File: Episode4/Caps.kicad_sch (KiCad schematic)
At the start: 170 parts

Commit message: Worked on BOM
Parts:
- added C176, C177, C183: 470µF, Capacitor_SMD:CP_Elec_16x17.5, symbol Device:C_Polarized_US
- added C178, C179, C184, C188, C191: 1µF, Capacitor_SMD:C_0805_2012Metric_Pad1.18x1.45mm_HandSolder, symbol Device:C_Small
- added C180, C181, C182, C185, C186, C189, C192: .1µF, Capacitor_SMD:C_0805_2012Metric_Pad1.18x1.45mm_HandSolder, symbol Device:C_Small
- added C187, C190: 100µF, Capacitor_SMD:CP_Elec_10x7.7, symbol Device:C_Polarized_US
- added C6: 1000µF, Capacitor_SMD:CP_Elec_16x17.5, symbol Device:C_Polarized_US
- C10: renamed from C9; footprint Capacitor_THT:C_Disc_D3.4mm_W2.1mm_P2.50mm -> Capacitor_SMD:C_0805_2012Metric_Pad1.18x1.45mm_HandSolder; Manufacturer_Name (none) -> Samsung Electro-Mechanics; Manufacturer_Part_Number (none) -> CL21B104KBFNNNG
- C100: renamed from C99; footprint Capacitor_THT:C_Disc_D3.4mm_W2.1mm_P2.50mm -> Capacitor_SMD:C_0805_2012Metric_Pad1.18x1.45mm_HandSolder; Manufacturer_Name (none) -> Samsung Electro-Mechanics; Manufacturer_Part_Number (none) -> CL21B104KBFNNNG
- C101: renamed from C100; footprint Capacitor_THT:C_Disc_D3.4mm_W2.1mm_P2.50mm -> Capacitor_SMD:C_0805_2012Metric_Pad1.18x1.45mm_HandSolder; Manufacturer_Name (none) -> Samsung Electro-Mechanics; Manufacturer_Part_Number (none) -> CL21B104KBFNNNG
- C102: renamed from C101; footprint Capacitor_THT:C_Disc_D3.4mm_W2.1mm_P2.50mm -> Capacitor_SMD:C_0805_2012Metric_Pad1.18x1.45mm_HandSolder; Manufacturer_Name (none) -> Samsung Electro-Mechanics; Manufacturer_Part_Number (none) -> CL21B104KBFNNNG
- C103: renamed from C102; footprint Capacitor_THT:C_Disc_D3.4mm_W2.1mm_P2.50mm -> Capacitor_SMD:C_0805_2012Metric_Pad1.18x1.45mm_HandSolder; Manufacturer_Name (none) -> Samsung Electro-Mechanics; Manufacturer_Part_Number (none) -> CL21B104KBFNNNG
- C104: renamed from C103; footprint Capacitor_THT:C_Disc_D3.4mm_W2.1mm_P2.50mm -> Capacitor_SMD:C_0805_2012Metric_Pad1.18x1.45mm_HandSolder; Manufacturer_Name (none) -> Samsung Electro-Mechanics; Manufacturer_Part_Number (none) -> CL21B104KBFNNNG
- C105: renamed from C104; footprint Capacitor_THT:C_Disc_D3.4mm_W2.1mm_P2.50mm -> Capacitor_SMD:C_0805_2012Metric_Pad1.18x1.45mm_HandSolder; Manufacturer_Name (none) -> Samsung Electro-Mechanics; Manufacturer_Part_Number (none) -> CL21B104KBFNNNG
- C106: renamed from C105; footprint Capacitor_THT:C_Disc_D3.4mm_W2.1mm_P2.50mm -> Capacitor_SMD:C_0805_2012Metric_Pad1.18x1.45mm_HandSolder; Manufacturer_Name (none) -> Samsung Electro-Mechanics; Manufacturer_Part_Number (none) -> CL21B104KBFNNNG
- C107: renamed from C106; footprint Capacitor_THT:C_Disc_D3.4mm_W2.1mm_P2.50mm -> Capacitor_SMD:C_0805_2012Metric_Pad1.18x1.45mm_HandSolder; Manufacturer_Name (none) -> Samsung Electro-Mechanics; Manufacturer_Part_Number (none) -> CL21B104KBFNNNG
- C108: renamed from C107; footprint Capacitor_THT:C_Disc_D3.4mm_W2.1mm_P2.50mm -> Capacitor_SMD:C_0805_2012Metric_Pad1.18x1.45mm_HandSolder; Manufacturer_Name (none) -> Samsung Electro-Mechanics; Manufacturer_Part_Number (none) -> CL21B104KBFNNNG
- C109: renamed from C108; footprint Capacitor_THT:C_Disc_D3.4mm_W2.1mm_P2.50mm -> Capacitor_SMD:C_0805_2012Metric_Pad1.18x1.45mm_HandSolder; Manufacturer_Name (none) -> Samsung Electro-Mechanics; Manufacturer_Part_Number (none) -> CL21B104KBFNNNG
- C11: renamed from C10; footprint Capacitor_THT:C_Disc_D3.4mm_W2.1mm_P2.50mm -> Capacitor_SMD:C_0805_2012Metric_Pad1.18x1.45mm_HandSolder; Manufacturer_Name (none) -> Samsung Electro-Mechanics; Manufacturer_Part_Number (none) -> CL21B104KBFNNNG
- C110: renamed from C109; footprint Capacitor_THT:C_Disc_D3.4mm_W2.1mm_P2.50mm -> Capacitor_SMD:C_0805_2012Metric_Pad1.18x1.45mm_HandSolder; Manufacturer_Name (none) -> Samsung Electro-Mechanics; Manufacturer_Part_Number (none) -> CL21B104KBFNNNG
- C111: renamed from C110; footprint Capacitor_THT:C_Disc_D3.4mm_W2.1mm_P2.50mm -> Capacitor_SMD:C_0805_2012Metric_Pad1.18x1.45mm_HandSolder; Manufacturer_Name (none) -> Samsung Electro-Mechanics; Manufacturer_Part_Number (none) -> CL21B104KBFNNNG
- C112: renamed from C111; footprint Capacitor_THT:C_Disc_D3.4mm_W2.1mm_P2.50mm -> Capacitor_SMD:C_0805_2012Metric_Pad1.18x1.45mm_HandSolder; Manufacturer_Name (none) -> Samsung Electro-Mechanics; Manufacturer_Part_Number (none) -> CL21B104KBFNNNG
- C113: renamed from C112; footprint Capacitor_THT:C_Disc_D3.4mm_W2.1mm_P2.50mm -> Capacitor_SMD:C_0805_2012Metric_Pad1.18x1.45mm_HandSolder; Manufacturer_Name (none) -> Samsung Electro-Mechanics; Manufacturer_Part_Number (none) -> CL21B104KBFNNNG
- C114: renamed from C113; footprint Capacitor_THT:C_Disc_D3.4mm_W2.1mm_P2.50mm -> Capacitor_SMD:C_0805_2012Metric_Pad1.18x1.45mm_HandSolder; Manufacturer_Name (none) -> Samsung Electro-Mechanics; Manufacturer_Part_Number (none) -> CL21B104KBFNNNG
- C115: renamed from C114; footprint Capacitor_THT:C_Disc_D3.4mm_W2.1mm_P2.50mm -> Capacitor_SMD:C_0805_2012Metric_Pad1.18x1.45mm_HandSolder; Manufacturer_Name (none) -> Samsung Electro-Mechanics; Manufacturer_Part_Number (none) -> CL21B104KBFNNNG
- C116: renamed from C115; footprint Capacitor_THT:C_Disc_D3.4mm_W2.1mm_P2.50mm -> Capacitor_SMD:C_0805_2012Metric_Pad1.18x1.45mm_HandSolder; Manufacturer_Name (none) -> Samsung Electro-Mechanics; Manufacturer_Part_Number (none) -> CL21B104KBFNNNG
- C117: renamed from C116; footprint Capacitor_THT:C_Disc_D3.4mm_W2.1mm_P2.50mm -> Capacitor_SMD:C_0805_2012Metric_Pad1.18x1.45mm_HandSolder; Manufacturer_Name (none) -> Samsung Electro-Mechanics; Manufacturer_Part_Number (none) -> CL21B104KBFNNNG
- C118: renamed from C117; footprint Capacitor_THT:C_Disc_D3.4mm_W2.1mm_P2.50mm -> Capacitor_SMD:C_0805_2012Metric_Pad1.18x1.45mm_HandSolder; Manufacturer_Name (none) -> Samsung Electro-Mechanics; Manufacturer_Part_Number (none) -> CL21B104KBFNNNG
- C119: renamed from C118; footprint Capacitor_THT:C_Disc_D3.4mm_W2.1mm_P2.50mm -> Capacitor_SMD:C_0805_2012Metric_Pad1.18x1.45mm_HandSolder; Manufacturer_Name (none) -> Samsung Electro-Mechanics; Manufacturer_Part_Number (none) -> CL21B104KBFNNNG
- C12: renamed from C11; value 100µF -> 470µF; footprint Capacitor_THT:CP_Radial_D6.3mm_P2.50mm -> Capacitor_SMD:CP_Elec_16x17.5; Manufacturer_Name (none) -> Nichicon; Manufacturer_Part_Number (none) -> UCD1H471MNJ1MS
- C120: renamed from C119; footprint Capacitor_THT:C_Disc_D3.4mm_W2.1mm_P2.50mm -> Capacitor_SMD:C_0805_2012Metric_Pad1.18x1.45mm_HandSolder; Manufacturer_Name (none) -> Samsung Electro-Mechanics; Manufacturer_Part_Number (none) -> CL21B104KBFNNNG
- C121: renamed from C120; footprint Capacitor_THT:C_Disc_D3.4mm_W2.1mm_P2.50mm -> Capacitor_SMD:C_0805_2012Metric_Pad1.18x1.45mm_HandSolder; Manufacturer_Name (none) -> Samsung Electro-Mechanics; Manufacturer_Part_Number (none) -> CL21B104KBFNNNG
- C122: renamed from C121; footprint Capacitor_THT:C_Disc_D3.4mm_W2.1mm_P2.50mm -> Capacitor_SMD:C_0805_2012Metric_Pad1.18x1.45mm_HandSolder; Manufacturer_Name (none) -> Samsung Electro-Mechanics; Manufacturer_Part_Number (none) -> CL21B104KBFNNNG
- C123: renamed from C122; footprint Capacitor_THT:C_Disc_D3.4mm_W2.1mm_P2.50mm -> Capacitor_SMD:C_0805_2012Metric_Pad1.18x1.45mm_HandSolder; Manufacturer_Name (none) -> Samsung Electro-Mechanics; Manufacturer_Part_Number (none) -> CL21B104KBFNNNG
- C124: renamed from C123; footprint Capacitor_THT:C_Disc_D3.4mm_W2.1mm_P2.50mm -> Capacitor_SMD:C_0805_2012Metric_Pad1.18x1.45mm_HandSolder; Manufacturer_Name (none) -> Samsung Electro-Mechanics; Manufacturer_Part_Number (none) -> CL21B104KBFNNNG
- C125: renamed from C124; footprint Capacitor_THT:C_Disc_D3.4mm_W2.1mm_P2.50mm -> Capacitor_SMD:C_0805_2012Metric_Pad1.18x1.45mm_HandSolder; Manufacturer_Name (none) -> Samsung Electro-Mechanics; Manufacturer_Part_Number (none) -> CL21B104KBFNNNG
- C126: renamed from C125; footprint Capacitor_THT:C_Disc_D3.4mm_W2.1mm_P2.50mm -> Capacitor_SMD:C_0805_2012Metric_Pad1.18x1.45mm_HandSolder; Manufacturer_Name (none) -> Samsung Electro-Mechanics; Manufacturer_Part_Number (none) -> CL21B104KBFNNNG
- C127: renamed from C126; footprint Capacitor_THT:C_Disc_D3.4mm_W2.1mm_P2.50mm -> Capacitor_SMD:C_0805_2012Metric_Pad1.18x1.45mm_HandSolder; Manufacturer_Name (none) -> Samsung Electro-Mechanics; Manufacturer_Part_Number (none) -> CL21B104KBFNNNG
- C128: renamed from C127; footprint Capacitor_THT:C_Disc_D3.4mm_W2.1mm_P2.50mm -> Capacitor_SMD:C_0805_2012Metric_Pad1.18x1.45mm_HandSolder; Manufacturer_Name (none) -> Samsung Electro-Mechanics; Manufacturer_Part_Number (none) -> CL21B104KBFNNNG
- C129: renamed from C128; footprint Capacitor_THT:C_Disc_D3.4mm_W2.1mm_P2.50mm -> Capacitor_SMD:C_0805_2012Metric_Pad1.18x1.45mm_HandSolder; Manufacturer_Name (none) -> Samsung Electro-Mechanics; Manufacturer_Part_Number (none) -> CL21B104KBFNNNG
- C13: renamed from C12; footprint Capacitor_THT:C_Disc_D3.4mm_W2.1mm_P2.50mm -> Capacitor_SMD:C_0805_2012Metric_Pad1.18x1.45mm_HandSolder; Manufacturer_Name (none) -> Samsung Electro-Mechanics; Manufacturer_Part_Number (none) -> CL21B105KBFNNNG
- C130: renamed from C129; footprint Capacitor_THT:C_Disc_D3.4mm_W2.1mm_P2.50mm -> Capacitor_SMD:C_0805_2012Metric_Pad1.18x1.45mm_HandSolder; Manufacturer_Name (none) -> Samsung Electro-Mechanics; Manufacturer_Part_Number (none) -> CL21B104KBFNNNG
- C131: renamed from C130; footprint Capacitor_THT:C_Disc_D3.4mm_W2.1mm_P2.50mm -> Capacitor_SMD:C_0805_2012Metric_Pad1.18x1.45mm_HandSolder; Manufacturer_Name (none) -> Samsung Electro-Mechanics; Manufacturer_Part_Number (none) -> CL21B104KBFNNNG
- C132: renamed from C131; footprint Capacitor_THT:C_Disc_D3.4mm_W2.1mm_P2.50mm -> Capacitor_SMD:C_0805_2012Metric_Pad1.18x1.45mm_HandSolder; Manufacturer_Name (none) -> Samsung Electro-Mechanics; Manufacturer_Part_Number (none) -> CL21B105KBFNNNG
- C133: renamed from C132; footprint Capacitor_THT:C_Disc_D3.4mm_W2.1mm_P2.50mm -> Capacitor_SMD:C_0805_2012Metric_Pad1.18x1.45mm_HandSolder; Manufacturer_Name (none) -> Samsung Electro-Mechanics; Manufacturer_Part_Number (none) -> CL21B105KBFNNNG
- C134: renamed from C133; footprint Capacitor_THT:C_Disc_D3.4mm_W2.1mm_P2.50mm -> Capacitor_SMD:C_0805_2012Metric_Pad1.18x1.45mm_HandSolder; Manufacturer_Name (none) -> Samsung Electro-Mechanics; Manufacturer_Part_Number (none) -> CL21B105KBFNNNG
- C135: renamed from C134; footprint Capacitor_THT:C_Disc_D3.4mm_W2.1mm_P2.50mm -> Capacitor_SMD:C_0805_2012Metric_Pad1.18x1.45mm_HandSolder; Manufacturer_Name (none) -> Samsung Electro-Mechanics; Manufacturer_Part_Number (none) -> CL21B105KBFNNNG
- C136: renamed from C135; footprint Capacitor_THT:C_Disc_D3.4mm_W2.1mm_P2.50mm -> Capacitor_SMD:C_0805_2012Metric_Pad1.18x1.45mm_HandSolder; Manufacturer_Name (none) -> Samsung Electro-Mechanics; Manufacturer_Part_Number (none) -> CL21B105KBFNNNG
- C137: renamed from C136; footprint Capacitor_THT:C_Disc_D3.4mm_W2.1mm_P2.50mm -> Capacitor_SMD:C_0805_2012Metric_Pad1.18x1.45mm_HandSolder; Manufacturer_Name (none) -> Samsung Electro-Mechanics; Manufacturer_Part_Number (none) -> CL21B105KBFNNNG
- C138: renamed from C137; footprint Capacitor_THT:C_Disc_D3.4mm_W2.1mm_P2.50mm -> Capacitor_SMD:C_0805_2012Metric_Pad1.18x1.45mm_HandSolder; Manufacturer_Name (none) -> Samsung Electro-Mechanics; Manufacturer_Part_Number (none) -> CL21B105KBFNNNG
- C139: renamed from C138; footprint Capacitor_THT:C_Disc_D3.4mm_W2.1mm_P2.50mm -> Capacitor_SMD:C_0805_2012Metric_Pad1.18x1.45mm_HandSolder; Manufacturer_Name (none) -> Samsung Electro-Mechanics; Manufacturer_Part_Number (none) -> CL21B105KBFNNNG
- C14: renamed from C13; footprint Capacitor_THT:C_Disc_D3.4mm_W2.1mm_P2.50mm -> Capacitor_SMD:C_0805_2012Metric_Pad1.18x1.45mm_HandSolder; Manufacturer_Name (none) -> Samsung Electro-Mechanics; Manufacturer_Part_Number (none) -> CL21B104KBFNNNG
- C140: renamed from C139; footprint Capacitor_THT:C_Disc_D3.4mm_W2.1mm_P2.50mm -> Capacitor_SMD:C_0805_2012Metric_Pad1.18x1.45mm_HandSolder; Manufacturer_Name (none) -> Samsung Electro-Mechanics; Manufacturer_Part_Number (none) -> CL21B105KBFNNNG
- C141: renamed from C140; footprint Capacitor_THT:C_Disc_D3.4mm_W2.1mm_P2.50mm -> Capacitor_SMD:C_0805_2012Metric_Pad1.18x1.45mm_HandSolder; Manufacturer_Name (none) -> Samsung Electro-Mechanics; Manufacturer_Part_Number (none) -> CL21B105KBFNNNG
- C142: renamed from C141; footprint Capacitor_THT:C_Disc_D3.4mm_W2.1mm_P2.50mm -> Capacitor_SMD:C_0805_2012Metric_Pad1.18x1.45mm_HandSolder; Manufacturer_Name (none) -> Samsung Electro-Mechanics; Manufacturer_Part_Number (none) -> CL21B105KBFNNNG
- C143: renamed from C142; footprint Capacitor_THT:C_Disc_D3.4mm_W2.1mm_P2.50mm -> Capacitor_SMD:C_0805_2012Metric_Pad1.18x1.45mm_HandSolder; Manufacturer_Name (none) -> Samsung Electro-Mechanics; Manufacturer_Part_Number (none) -> CL21B104KBFNNNG
- C144: renamed from C143; footprint Capacitor_THT:C_Disc_D3.4mm_W2.1mm_P2.50mm -> Capacitor_SMD:C_0805_2012Metric_Pad1.18x1.45mm_HandSolder; Manufacturer_Name (none) -> Samsung Electro-Mechanics; Manufacturer_Part_Number (none) -> CL21B104KBFNNNG
- C145: renamed from C144; footprint Capacitor_THT:C_Disc_D3.4mm_W2.1mm_P2.50mm -> Capacitor_SMD:C_0805_2012Metric_Pad1.18x1.45mm_HandSolder; Manufacturer_Name (none) -> Samsung Electro-Mechanics; Manufacturer_Part_Number (none) -> CL21B104KBFNNNG
- C146: renamed from C145; footprint Capacitor_THT:C_Disc_D3.4mm_W2.1mm_P2.50mm -> Capacitor_SMD:C_0805_2012Metric_Pad1.18x1.45mm_HandSolder; Manufacturer_Name (none) -> Samsung Electro-Mechanics; Manufacturer_Part_Number (none) -> CL21B104KBFNNNG
- C147: renamed from C146; footprint Capacitor_THT:C_Disc_D3.4mm_W2.1mm_P2.50mm -> Capacitor_SMD:C_0805_2012Metric_Pad1.18x1.45mm_HandSolder; Manufacturer_Name (none) -> Samsung Electro-Mechanics; Manufacturer_Part_Number (none) -> CL21B104KBFNNNG
- C148: renamed from C147; footprint Capacitor_THT:C_Disc_D3.4mm_W2.1mm_P2.50mm -> Capacitor_SMD:C_0805_2012Metric_Pad1.18x1.45mm_HandSolder; Manufacturer_Name (none) -> Samsung Electro-Mechanics; Manufacturer_Part_Number (none) -> CL21B104KBFNNNG
- C149: renamed from C148; footprint Capacitor_THT:C_Disc_D3.4mm_W2.1mm_P2.50mm -> Capacitor_SMD:C_0805_2012Metric_Pad1.18x1.45mm_HandSolder; Manufacturer_Name (none) -> Samsung Electro-Mechanics; Manufacturer_Part_Number (none) -> CL21B104KBFNNNG
- C15: renamed from C14; footprint Capacitor_THT:C_Disc_D3.4mm_W2.1mm_P2.50mm -> Capacitor_SMD:C_0805_2012Metric_Pad1.18x1.45mm_HandSolder; Manufacturer_Name (none) -> Samsung Electro-Mechanics; Manufacturer_Part_Number (none) -> CL21B104KBFNNNG
- C150: renamed from C149; footprint Capacitor_THT:C_Disc_D3.4mm_W2.1mm_P2.50mm -> Capacitor_SMD:C_0805_2012Metric_Pad1.18x1.45mm_HandSolder; Manufacturer_Name (none) -> Samsung Electro-Mechanics; Manufacturer_Part_Number (none) -> CL21B104KBFNNNG
- C151: renamed from C150; footprint Capacitor_THT:C_Disc_D3.4mm_W2.1mm_P2.50mm -> Capacitor_SMD:C_0805_2012Metric_Pad1.18x1.45mm_HandSolder; Manufacturer_Name (none) -> Samsung Electro-Mechanics; Manufacturer_Part_Number (none) -> CL21B104KBFNNNG
- C152: renamed from C151; footprint Capacitor_THT:C_Disc_D3.4mm_W2.1mm_P2.50mm -> Capacitor_SMD:C_0805_2012Metric_Pad1.18x1.45mm_HandSolder; Manufacturer_Name (none) -> Samsung Electro-Mechanics; Manufacturer_Part_Number (none) -> CL21B104KBFNNNG
- C153: renamed from C152; footprint Capacitor_THT:C_Disc_D3.4mm_W2.1mm_P2.50mm -> Capacitor_SMD:C_0805_2012Metric_Pad1.18x1.45mm_HandSolder; Manufacturer_Name (none) -> Samsung Electro-Mechanics; Manufacturer_Part_Number (none) -> CL21B104KBFNNNG
- C154: renamed from C153; footprint Capacitor_THT:C_Disc_D3.4mm_W2.1mm_P2.50mm -> Capacitor_SMD:C_0805_2012Metric_Pad1.18x1.45mm_HandSolder; Manufacturer_Name (none) -> Samsung Electro-Mechanics; Manufacturer_Part_Number (none) -> CL21B105KBFNNNG
- C155: renamed from C154; footprint Capacitor_THT:C_Disc_D3.4mm_W2.1mm_P2.50mm -> Capacitor_SMD:C_0805_2012Metric_Pad1.18x1.45mm_HandSolder; Manufacturer_Name (none) -> Samsung Electro-Mechanics; Manufacturer_Part_Number (none) -> CL21B105KBFNNNG
- C156: renamed from C155; footprint Capacitor_THT:C_Disc_D3.4mm_W2.1mm_P2.50mm -> Capacitor_SMD:C_0805_2012Metric_Pad1.18x1.45mm_HandSolder; Manufacturer_Name (none) -> Samsung Electro-Mechanics; Manufacturer_Part_Number (none) -> CL21B105KBFNNNG
- C157: renamed from C156; footprint Capacitor_THT:C_Disc_D3.4mm_W2.1mm_P2.50mm -> Capacitor_SMD:C_0805_2012Metric_Pad1.18x1.45mm_HandSolder; Manufacturer_Name (none) -> Samsung Electro-Mechanics; Manufacturer_Part_Number (none) -> CL21B105KBFNNNG
- C158: renamed from C157; footprint Capacitor_THT:C_Disc_D3.4mm_W2.1mm_P2.50mm -> Capacitor_SMD:C_0805_2012Metric_Pad1.18x1.45mm_HandSolder; Manufacturer_Name (none) -> Samsung Electro-Mechanics; Manufacturer_Part_Number (none) -> CL21B105KBFNNNG
- C159: renamed from C158; footprint Capacitor_THT:C_Disc_D3.4mm_W2.1mm_P2.50mm -> Capacitor_SMD:C_0805_2012Metric_Pad1.18x1.45mm_HandSolder; Manufacturer_Name (none) -> Samsung Electro-Mechanics; Manufacturer_Part_Number (none) -> CL21B105KBFNNNG
- C16: renamed from C15; footprint Capacitor_THT:CP_Radial_D6.3mm_P2.50mm -> Capacitor_SMD:CP_Elec_10x7.7; Manufacturer_Name (none) -> Nichicon; Manufacturer_Part_Number (none) -> UCD1H101MCL6GS
- C160: renamed from C159; footprint Capacitor_THT:C_Disc_D3.4mm_W2.1mm_P2.50mm -> Capacitor_SMD:C_0805_2012Metric_Pad1.18x1.45mm_HandSolder; Manufacturer_Name (none) -> Samsung Electro-Mechanics; Manufacturer_Part_Number (none) -> CL21B105KBFNNNG
- C161: renamed from C160; footprint Capacitor_THT:C_Disc_D3.4mm_W2.1mm_P2.50mm -> Capacitor_SMD:C_0805_2012Metric_Pad1.18x1.45mm_HandSolder; Manufacturer_Name (none) -> Samsung Electro-Mechanics; Manufacturer_Part_Number (none) -> CL21B105KBFNNNG
- C162: renamed from C161; footprint Capacitor_THT:C_Disc_D3.4mm_W2.1mm_P2.50mm -> Capacitor_SMD:C_0805_2012Metric_Pad1.18x1.45mm_HandSolder; Manufacturer_Name (none) -> Samsung Electro-Mechanics; Manufacturer_Part_Number (none) -> CL21B105KBFNNNG
- C163: renamed from C162; footprint Capacitor_THT:C_Disc_D3.4mm_W2.1mm_P2.50mm -> Capacitor_SMD:C_0805_2012Metric_Pad1.18x1.45mm_HandSolder; Manufacturer_Name (none) -> Samsung Electro-Mechanics; Manufacturer_Part_Number (none) -> CL21B105KBFNNNG
- C164: renamed from C163; footprint Capacitor_THT:C_Disc_D3.4mm_W2.1mm_P2.50mm -> Capacitor_SMD:C_0805_2012Metric_Pad1.18x1.45mm_HandSolder; Manufacturer_Name (none) -> Samsung Electro-Mechanics; Manufacturer_Part_Number (none) -> CL21B105KBFNNNG
- C165: renamed from C164; footprint Capacitor_THT:C_Disc_D3.4mm_W2.1mm_P2.50mm -> Capacitor_SMD:C_0805_2012Metric_Pad1.18x1.45mm_HandSolder; Manufacturer_Name (none) -> Samsung Electro-Mechanics; Manufacturer_Part_Number (none) -> CL21B104KBFNNNG
- C166: renamed from C165; footprint Capacitor_THT:C_Disc_D3.4mm_W2.1mm_P2.50mm -> Capacitor_SMD:C_0805_2012Metric_Pad1.18x1.45mm_HandSolder; Manufacturer_Name (none) -> Samsung Electro-Mechanics; Manufacturer_Part_Number (none) -> CL21B104KBFNNNG
- C167: renamed from C166; footprint Capacitor_THT:C_Disc_D3.4mm_W2.1mm_P2.50mm -> Capacitor_SMD:C_0805_2012Metric_Pad1.18x1.45mm_HandSolder; Manufacturer_Name (none) -> Samsung Electro-Mechanics; Manufacturer_Part_Number (none) -> CL21B104KBFNNNG
- C168: renamed from C167; footprint Capacitor_THT:C_Disc_D3.4mm_W2.1mm_P2.50mm -> Capacitor_SMD:C_0805_2012Metric_Pad1.18x1.45mm_HandSolder; Manufacturer_Name (none) -> Samsung Electro-Mechanics; Manufacturer_Part_Number (none) -> CL21B104KBFNNNG
- C169: renamed from C168; footprint Capacitor_THT:C_Disc_D3.4mm_W2.1mm_P2.50mm -> Capacitor_SMD:C_0805_2012Metric_Pad1.18x1.45mm_HandSolder; Manufacturer_Name (none) -> Samsung Electro-Mechanics; Manufacturer_Part_Number (none) -> CL21B104KBFNNNG
- C17: renamed from C16; footprint Capacitor_THT:C_Disc_D3.4mm_W2.1mm_P2.50mm -> Capacitor_SMD:C_0805_2012Metric_Pad1.18x1.45mm_HandSolder; Manufacturer_Name (none) -> Samsung Electro-Mechanics; Manufacturer_Part_Number (none) -> CL21B105KBFNNNG
- C170: renamed from C169; footprint Capacitor_THT:C_Disc_D3.4mm_W2.1mm_P2.50mm -> Capacitor_SMD:C_0805_2012Metric_Pad1.18x1.45mm_HandSolder; Manufacturer_Name (none) -> Samsung Electro-Mechanics; Manufacturer_Part_Number (none) -> CL21B104KBFNNNG
- C171: renamed from C170; footprint Capacitor_THT:C_Disc_D3.4mm_W2.1mm_P2.50mm -> Capacitor_SMD:C_0805_2012Metric_Pad1.18x1.45mm_HandSolder; Manufacturer_Name (none) -> Samsung Electro-Mechanics; Manufacturer_Part_Number (none) -> CL21B104KBFNNNG
- C172: renamed from C171; footprint Capacitor_THT:C_Disc_D3.4mm_W2.1mm_P2.50mm -> Capacitor_SMD:C_0805_2012Metric_Pad1.18x1.45mm_HandSolder; Manufacturer_Name (none) -> Samsung Electro-Mechanics; Manufacturer_Part_Number (none) -> CL21B104KBFNNNG
- C173: renamed from C172; footprint Capacitor_THT:C_Disc_D3.4mm_W2.1mm_P2.50mm -> Capacitor_SMD:C_0805_2012Metric_Pad1.18x1.45mm_HandSolder; Manufacturer_Name (none) -> Samsung Electro-Mechanics; Manufacturer_Part_Number (none) -> CL21B104KBFNNNG
- C174: renamed from C173; footprint Capacitor_THT:C_Disc_D3.4mm_W2.1mm_P2.50mm -> Capacitor_SMD:C_0805_2012Metric_Pad1.18x1.45mm_HandSolder; Manufacturer_Name (none) -> Samsung Electro-Mechanics; Manufacturer_Part_Number (none) -> CL21B104KBFNNNG
- C175: renamed from C174; footprint Capacitor_THT:C_Disc_D3.4mm_W2.1mm_P2.50mm -> Capacitor_SMD:C_0805_2012Metric_Pad1.18x1.45mm_HandSolder; Manufacturer_Name (none) -> Samsung Electro-Mechanics; Manufacturer_Part_Number (none) -> CL21B104KBFNNNG
- C18: renamed from C17; footprint Capacitor_THT:C_Disc_D3.4mm_W2.1mm_P2.50mm -> Capacitor_SMD:C_0805_2012Metric_Pad1.18x1.45mm_HandSolder; Manufacturer_Name (none) -> Samsung Electro-Mechanics; Manufacturer_Part_Number (none) -> CL21B104KBFNNNG
- C19: renamed from C18; footprint Capacitor_THT:CP_Radial_D6.3mm_P2.50mm -> Capacitor_SMD:CP_Elec_10x7.7; Manufacturer_Name (none) -> Nichicon; Manufacturer_Part_Number (none) -> UCD1H101MCL6GS
- C20: renamed from C19; footprint Capacitor_THT:C_Disc_D3.4mm_W2.1mm_P2.50mm -> Capacitor_SMD:C_0805_2012Metric_Pad1.18x1.45mm_HandSolder; Manufacturer_Name (none) -> Samsung Electro-Mechanics; Manufacturer_Part_Number (none) -> CL21B105KBFNNNG
- C21: renamed from C20; footprint Capacitor_THT:C_Disc_D3.4mm_W2.1mm_P2.50mm -> Capacitor_SMD:C_0805_2012Metric_Pad1.18x1.45mm_HandSolder; Manufacturer_Name (none) -> Samsung Electro-Mechanics; Manufacturer_Part_Number (none) -> CL21B104KBFNNNG
- C22: renamed from C21; footprint Capacitor_THT:CP_Radial_D5.0mm_P2.50mm -> Capacitor_SMD:CP_Elec_6.3x5.8; Manufacturer_Name (none) -> Nichicon; Manufacturer_Part_Number (none) -> UCD1H100MCL6GS
- C23: renamed from C22; footprint Capacitor_THT:CP_Radial_D5.0mm_P2.50mm -> Capacitor_SMD:CP_Elec_6.3x5.8; Manufacturer_Name (none) -> Nichicon; Manufacturer_Part_Number (none) -> UCD1H100MCL6GS
- C24: renamed from C23; footprint Capacitor_THT:CP_Radial_D5.0mm_P2.50mm -> Capacitor_SMD:CP_Elec_6.3x5.8; Manufacturer_Name (none) -> Nichicon; Manufacturer_Part_Number (none) -> UCD1H100MCL6GS
- C25: renamed from C24; footprint Capacitor_THT:CP_Radial_D5.0mm_P2.50mm -> Capacitor_SMD:CP_Elec_6.3x5.8; Manufacturer_Name (none) -> Nichicon; Manufacturer_Part_Number (none) -> UCD1H100MCL6GS
- C26: renamed from C25; footprint Capacitor_THT:CP_Radial_D5.0mm_P2.50mm -> Capacitor_SMD:CP_Elec_6.3x5.8; Manufacturer_Name (none) -> Nichicon; Manufacturer_Part_Number (none) -> UCD1H100MCL6GS
- C27: renamed from C26; footprint Capacitor_THT:CP_Radial_D5.0mm_P2.50mm -> Capacitor_SMD:CP_Elec_6.3x5.8; Manufacturer_Name (none) -> Nichicon; Manufacturer_Part_Number (none) -> UCD1H100MCL6GS
- C28: renamed from C27; footprint Capacitor_THT:CP_Radial_D5.0mm_P2.50mm -> Capacitor_SMD:CP_Elec_6.3x5.8; Manufacturer_Name (none) -> Nichicon; Manufacturer_Part_Number (none) -> UCD1H100MCL6GS
- C29: renamed from C28; footprint Capacitor_THT:CP_Radial_D5.0mm_P2.50mm -> Capacitor_SMD:CP_Elec_6.3x5.8; Manufacturer_Name (none) -> Nichicon; Manufacturer_Part_Number (none) -> UCD1H100MCL6GS
- C30: renamed from C29; footprint Capacitor_THT:CP_Radial_D5.0mm_P2.50mm -> Capacitor_SMD:CP_Elec_6.3x5.8; Manufacturer_Name (none) -> Nichicon; Manufacturer_Part_Number (none) -> UCD1H100MCL6GS
- C31: renamed from C30; footprint Capacitor_THT:CP_Radial_D5.0mm_P2.50mm -> Capacitor_SMD:CP_Elec_6.3x5.8; Manufacturer_Name (none) -> Nichicon; Manufacturer_Part_Number (none) -> UCD1H100MCL6GS
- C32: renamed from C31; footprint Capacitor_THT:CP_Radial_D5.0mm_P2.50mm -> Capacitor_SMD:CP_Elec_6.3x5.8; Manufacturer_Name (none) -> Nichicon; Manufacturer_Part_Number (none) -> UCD1H100MCL6GS
- C33: renamed from C32; footprint Capacitor_THT:CP_Radial_D5.0mm_P2.50mm -> Capacitor_SMD:CP_Elec_6.3x5.8; Manufacturer_Name (none) -> Nichicon; Manufacturer_Part_Number (none) -> UCD1H100MCL6GS
- C34: renamed from C33; footprint Capacitor_THT:CP_Radial_D5.0mm_P2.50mm -> Capacitor_SMD:CP_Elec_6.3x5.8; Manufacturer_Name (none) -> Nichicon; Manufacturer_Part_Number (none) -> UCD1H100MCL6GS
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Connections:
- net +12V: now also C187.1, C188.1, C189.1
- net +3V3: now also C183.1, C184.1, C185.1, C186.1
- net +5V: now also C176.1, C177.1, C178.1, C179.1, C180.1, C181.1, C182.1, C6.1
- net -12V: now also C190.2, C191.1, C192.1
- net GND: now also C176.2, C177.2, C178.2, C179.2, C180.2, C181.2, C182.2, C183.2, C184.2, C185.2, C186.2, C187.2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
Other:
- note added: "END CAPACITORS"
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
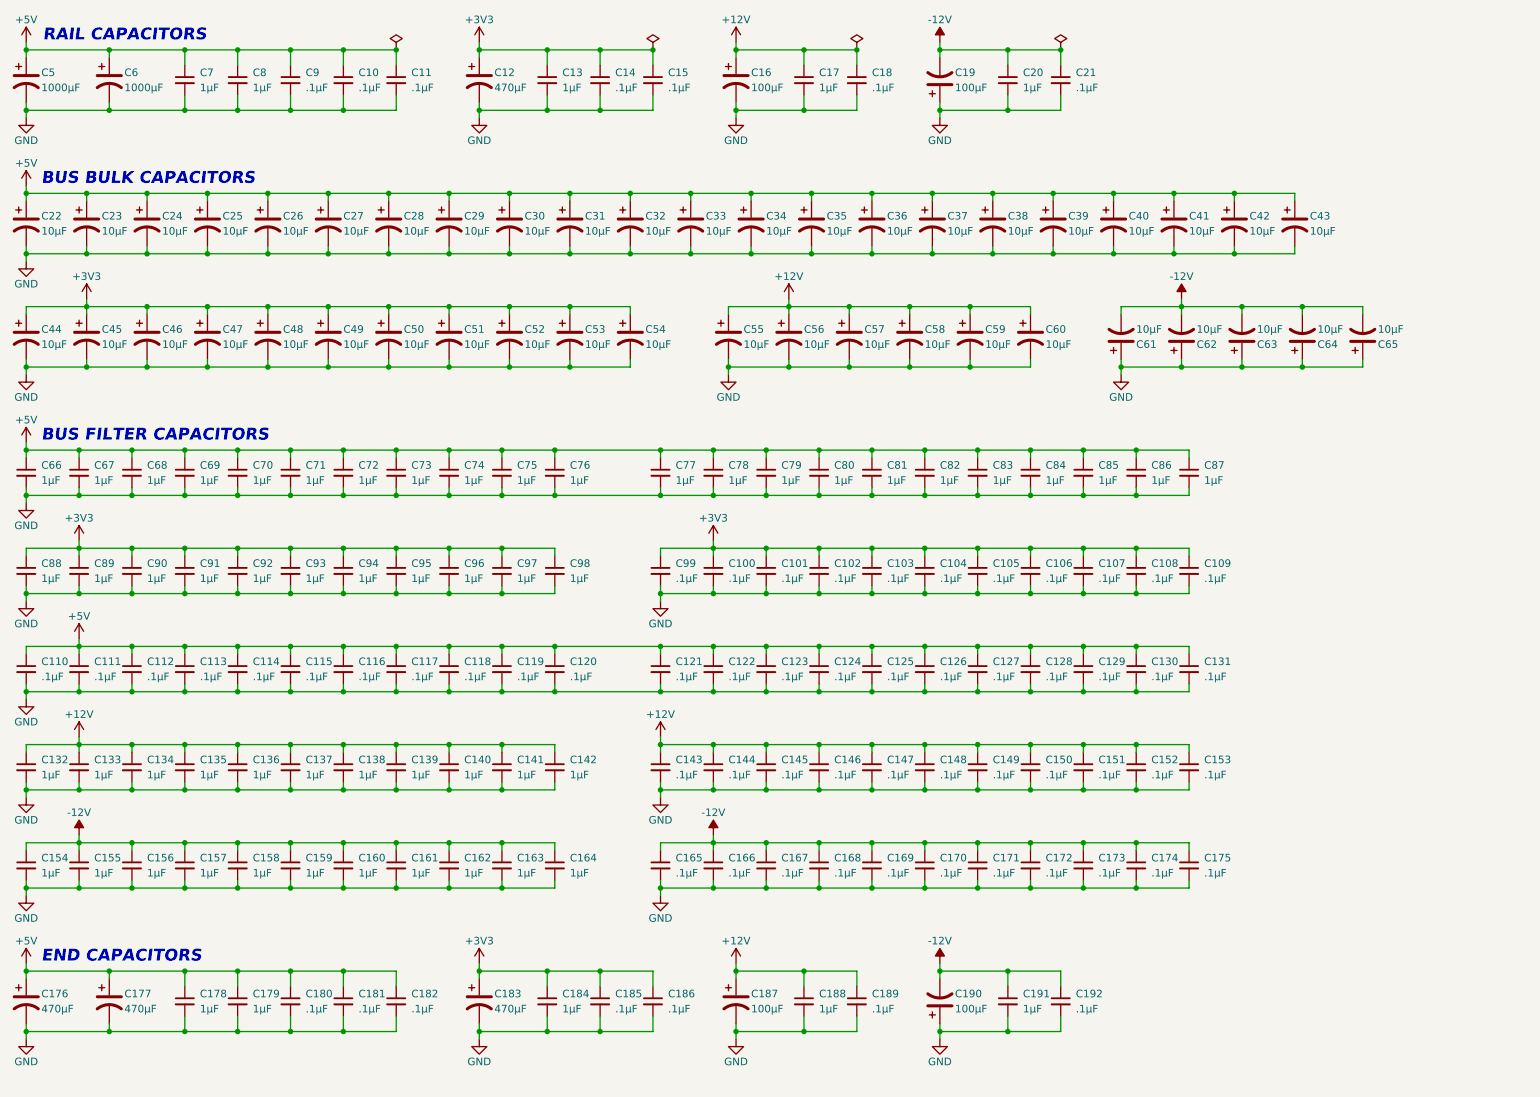
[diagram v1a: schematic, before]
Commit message: Changed bus from 62 to 72 pins
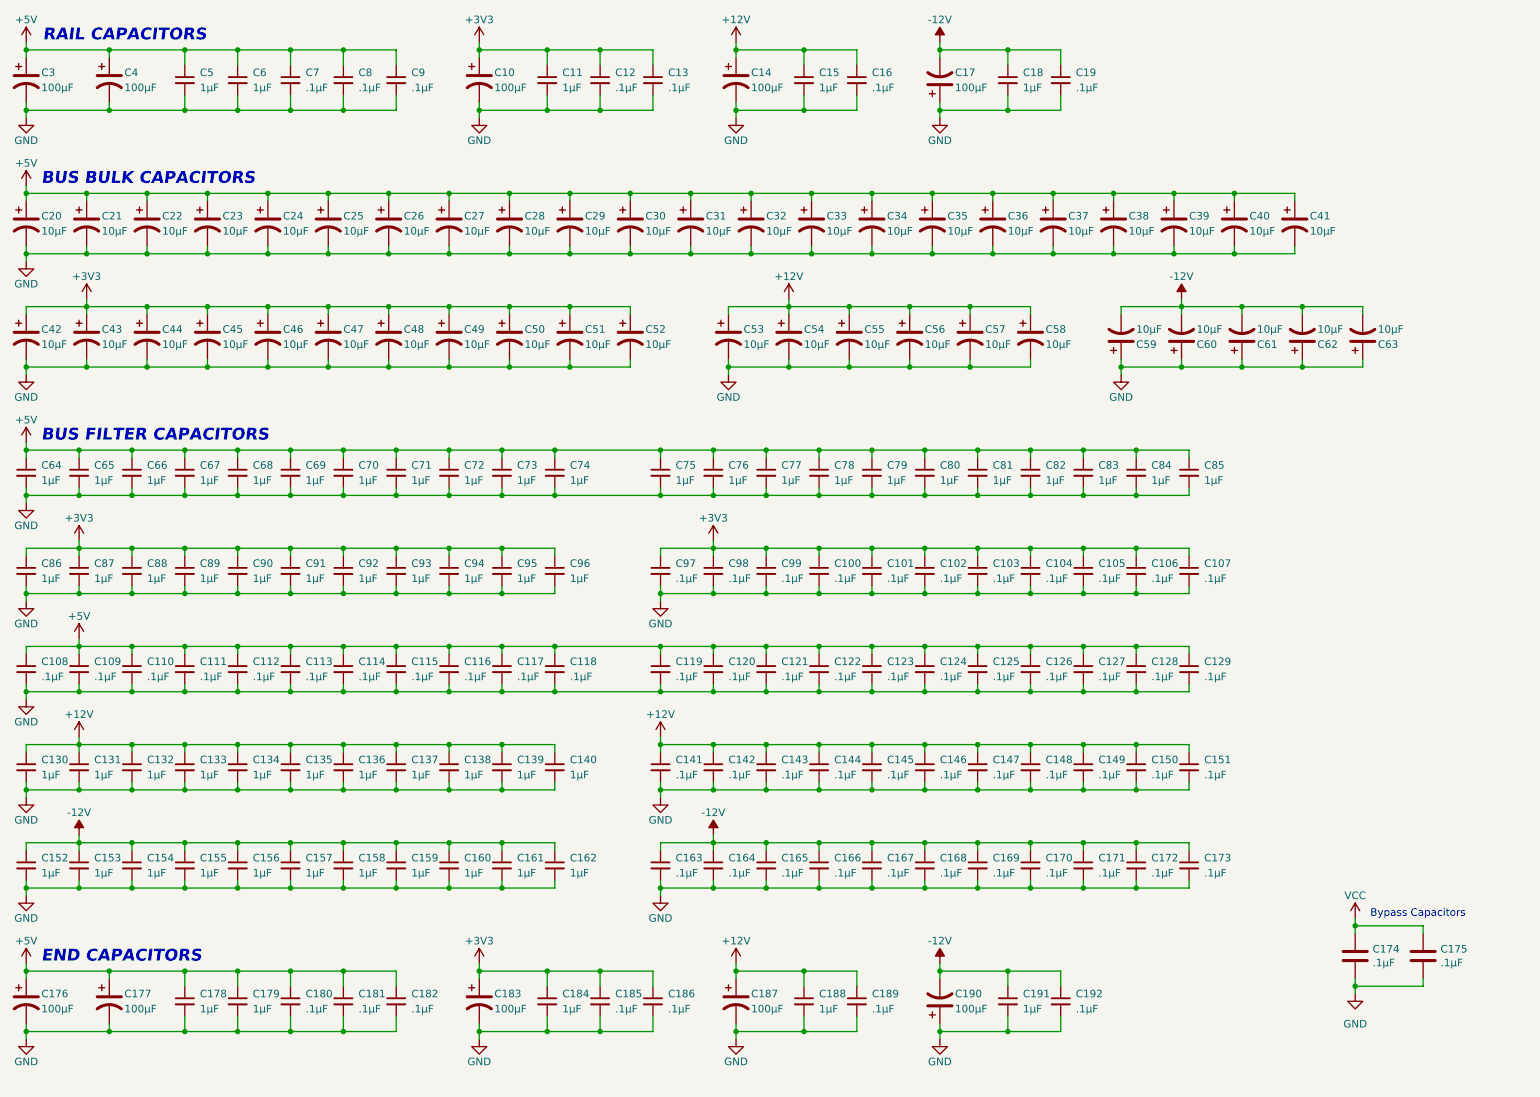
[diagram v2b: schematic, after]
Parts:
- added C174, C175: .1µF, Capacitor_SMD:C_0805_2012Metric_Pad1.18x1.45mm_HandSolder, symbol Device:C
- C10: renamed from C12; value 470µF -> 100µF; footprint Capacitor_SMD:CP_Elec_16x17.5 -> Capacitor_SMD:CP_Elec_6.3x7.7; Manufacturer_Part_Number UCD1H471MNJ1MS -> UCD1E101MCL1GS
- C14: renamed from C16; footprint Capacitor_SMD:CP_Elec_10x7.7 -> Capacitor_SMD:CP_Elec_6.3x7.7; Manufacturer_Part_Number UCD1H101MCL6GS -> UCD1E101MCL1GS
- C17: renamed from C19; footprint Capacitor_SMD:CP_Elec_10x7.7 -> Capacitor_SMD:CP_Elec_6.3x7.7; Manufacturer_Part_Number UCD1H101MCL6GS -> UCD1E101MCL1GS
- C176, C177, C183: value 470µF -> 100µF; footprint Capacitor_SMD:CP_Elec_16x17.5 -> Capacitor_SMD:CP_Elec_6.3x7.7; Manufacturer_Part_Number UCD1H471MNJ1MS -> UCD1E101MCL1GS
- C187, C190: footprint Capacitor_SMD:CP_Elec_10x7.7 -> Capacitor_SMD:CP_Elec_6.3x7.7; Manufacturer_Part_Number UCD1H101MCL6GS -> UCD1E101MCL1GS
- C20: renamed from C22; footprint Capacitor_SMD:CP_Elec_6.3x5.8 -> Capacitor_SMD:CP_Elec_4x5.8; Manufacturer_Part_Number UCD1H100MCL6GS -> UCD1E100MCL1GS
- C21: renamed from C23; footprint Capacitor_SMD:CP_Elec_6.3x5.8 -> Capacitor_SMD:CP_Elec_4x5.8; Manufacturer_Part_Number UCD1H100MCL6GS -> UCD1E100MCL1GS
- C22: renamed from C24; footprint Capacitor_SMD:CP_Elec_6.3x5.8 -> Capacitor_SMD:CP_Elec_4x5.8; Manufacturer_Part_Number UCD1H100MCL6GS -> UCD1E100MCL1GS
- C23: renamed from C25; footprint Capacitor_SMD:CP_Elec_6.3x5.8 -> Capacitor_SMD:CP_Elec_4x5.8; Manufacturer_Part_Number UCD1H100MCL6GS -> UCD1E100MCL1GS
- C24: renamed from C26; footprint Capacitor_SMD:CP_Elec_6.3x5.8 -> Capacitor_SMD:CP_Elec_4x5.8; Manufacturer_Part_Number UCD1H100MCL6GS -> UCD1E100MCL1GS
- C25: renamed from C27; footprint Capacitor_SMD:CP_Elec_6.3x5.8 -> Capacitor_SMD:CP_Elec_4x5.8; Manufacturer_Part_Number UCD1H100MCL6GS -> UCD1E100MCL1GS
- C26: renamed from C28; footprint Capacitor_SMD:CP_Elec_6.3x5.8 -> Capacitor_SMD:CP_Elec_4x5.8; Manufacturer_Part_Number UCD1H100MCL6GS -> UCD1E100MCL1GS
- C27: renamed from C29; footprint Capacitor_SMD:CP_Elec_6.3x5.8 -> Capacitor_SMD:CP_Elec_4x5.8; Manufacturer_Part_Number UCD1H100MCL6GS -> UCD1E100MCL1GS
- C28: renamed from C30; footprint Capacitor_SMD:CP_Elec_6.3x5.8 -> Capacitor_SMD:CP_Elec_4x5.8; Manufacturer_Part_Number UCD1H100MCL6GS -> UCD1E100MCL1GS
- C29: renamed from C31; footprint Capacitor_SMD:CP_Elec_6.3x5.8 -> Capacitor_SMD:CP_Elec_4x5.8; Manufacturer_Part_Number UCD1H100MCL6GS -> UCD1E100MCL1GS
- C3: renamed from C5; value 1000µF -> 100µF; footprint Capacitor_SMD:CP_Elec_16x17.5 -> Capacitor_SMD:CP_Elec_6.3x7.7; Manufacturer_Part_Number UCD1V102MNJ1MS -> UCD1E101MCL1GS
- C30: renamed from C32; footprint Capacitor_SMD:CP_Elec_6.3x5.8 -> Capacitor_SMD:CP_Elec_4x5.8; Manufacturer_Part_Number UCD1H100MCL6GS -> UCD1E100MCL1GS
- C31: renamed from C33; footprint Capacitor_SMD:CP_Elec_6.3x5.8 -> Capacitor_SMD:CP_Elec_4x5.8; Manufacturer_Part_Number UCD1H100MCL6GS -> UCD1E100MCL1GS
- C32: renamed from C34; footprint Capacitor_SMD:CP_Elec_6.3x5.8 -> Capacitor_SMD:CP_Elec_4x5.8; Manufacturer_Part_Number UCD1H100MCL6GS -> UCD1E100MCL1GS
- C33: renamed from C35; footprint Capacitor_SMD:CP_Elec_6.3x5.8 -> Capacitor_SMD:CP_Elec_4x5.8; Manufacturer_Part_Number UCD1H100MCL6GS -> UCD1E100MCL1GS
- C34: renamed from C36; footprint Capacitor_SMD:CP_Elec_6.3x5.8 -> Capacitor_SMD:CP_Elec_4x5.8; Manufacturer_Part_Number UCD1H100MCL6GS -> UCD1E100MCL1GS
- C35: renamed from C37; footprint Capacitor_SMD:CP_Elec_6.3x5.8 -> Capacitor_SMD:CP_Elec_4x5.8; Manufacturer_Part_Number UCD1H100MCL6GS -> UCD1E100MCL1GS
- C36: renamed from C38; footprint Capacitor_SMD:CP_Elec_6.3x5.8 -> Capacitor_SMD:CP_Elec_4x5.8; Manufacturer_Part_Number UCD1H100MCL6GS -> UCD1E100MCL1GS
- C37: renamed from C39; footprint Capacitor_SMD:CP_Elec_6.3x5.8 -> Capacitor_SMD:CP_Elec_4x5.8; Manufacturer_Part_Number UCD1H100MCL6GS -> UCD1E100MCL1GS
- C38: renamed from C40; footprint Capacitor_SMD:CP_Elec_6.3x5.8 -> Capacitor_SMD:CP_Elec_4x5.8; Manufacturer_Part_Number UCD1H100MCL6GS -> UCD1E100MCL1GS
- C39: renamed from C41; footprint Capacitor_SMD:CP_Elec_6.3x5.8 -> Capacitor_SMD:CP_Elec_4x5.8; Manufacturer_Part_Number UCD1H100MCL6GS -> UCD1E100MCL1GS
- C4: renamed from C6; value 1000µF -> 100µF; footprint Capacitor_SMD:CP_Elec_16x17.5 -> Capacitor_SMD:CP_Elec_6.3x7.7; Manufacturer_Part_Number UCD1V102MNJ1MS -> UCD1E101MCL1GS
- C40: renamed from C42; footprint Capacitor_SMD:CP_Elec_6.3x5.8 -> Capacitor_SMD:CP_Elec_4x5.8; Manufacturer_Part_Number UCD1H100MCL6GS -> UCD1E100MCL1GS
- C41: renamed from C43; footprint Capacitor_SMD:CP_Elec_6.3x5.8 -> Capacitor_SMD:CP_Elec_4x5.8; Manufacturer_Part_Number UCD1H100MCL6GS -> UCD1E100MCL1GS
- C42: renamed from C44; footprint Capacitor_SMD:CP_Elec_6.3x5.8 -> Capacitor_SMD:CP_Elec_4x5.8; Manufacturer_Part_Number UCD1H100MCL6GS -> UCD1E100MCL1GS
- C43: renamed from C45; footprint Capacitor_SMD:CP_Elec_6.3x5.8 -> Capacitor_SMD:CP_Elec_4x5.8; Manufacturer_Part_Number UCD1H100MCL6GS -> UCD1E100MCL1GS
- C44: renamed from C46; footprint Capacitor_SMD:CP_Elec_6.3x5.8 -> Capacitor_SMD:CP_Elec_4x5.8; Manufacturer_Part_Number UCD1H100MCL6GS -> UCD1E100MCL1GS
- C45: renamed from C47; footprint Capacitor_SMD:CP_Elec_6.3x5.8 -> Capacitor_SMD:CP_Elec_4x5.8; Manufacturer_Part_Number UCD1H100MCL6GS -> UCD1E100MCL1GS
- C46: renamed from C48; footprint Capacitor_SMD:CP_Elec_6.3x5.8 -> Capacitor_SMD:CP_Elec_4x5.8; Manufacturer_Part_Number UCD1H100MCL6GS -> UCD1E100MCL1GS
- C47: renamed from C49; footprint Capacitor_SMD:CP_Elec_6.3x5.8 -> Capacitor_SMD:CP_Elec_4x5.8; Manufacturer_Part_Number UCD1H100MCL6GS -> UCD1E100MCL1GS
- C48: renamed from C50; footprint Capacitor_SMD:CP_Elec_6.3x5.8 -> Capacitor_SMD:CP_Elec_4x5.8; Manufacturer_Part_Number UCD1H100MCL6GS -> UCD1E100MCL1GS
- C49: renamed from C51; footprint Capacitor_SMD:CP_Elec_6.3x5.8 -> Capacitor_SMD:CP_Elec_4x5.8; Manufacturer_Part_Number UCD1H100MCL6GS -> UCD1E100MCL1GS
- C50: renamed from C52; footprint Capacitor_SMD:CP_Elec_6.3x5.8 -> Capacitor_SMD:CP_Elec_4x5.8; Manufacturer_Part_Number UCD1H100MCL6GS -> UCD1E100MCL1GS
- C51: renamed from C53; footprint Capacitor_SMD:CP_Elec_6.3x5.8 -> Capacitor_SMD:CP_Elec_4x5.8; Manufacturer_Part_Number UCD1H100MCL6GS -> UCD1E100MCL1GS
- C52: renamed from C54; footprint Capacitor_SMD:CP_Elec_6.3x5.8 -> Capacitor_SMD:CP_Elec_4x5.8; Manufacturer_Part_Number UCD1H100MCL6GS -> UCD1E100MCL1GS
- C53: renamed from C55; footprint Capacitor_SMD:CP_Elec_6.3x5.8 -> Capacitor_SMD:CP_Elec_4x5.8; Manufacturer_Part_Number UCD1H100MCL6GS -> UCD1E100MCL1GS
- C54: renamed from C56; footprint Capacitor_SMD:CP_Elec_6.3x5.8 -> Capacitor_SMD:CP_Elec_4x5.8; Manufacturer_Part_Number UCD1H100MCL6GS -> UCD1E100MCL1GS
- C55: renamed from C57; footprint Capacitor_SMD:CP_Elec_6.3x5.8 -> Capacitor_SMD:CP_Elec_4x5.8; Manufacturer_Part_Number UCD1H100MCL6GS -> UCD1E100MCL1GS
- C56: renamed from C58; footprint Capacitor_SMD:CP_Elec_6.3x5.8 -> Capacitor_SMD:CP_Elec_4x5.8; Manufacturer_Part_Number UCD1H100MCL6GS -> UCD1E100MCL1GS
- C57: renamed from C59; footprint Capacitor_SMD:CP_Elec_6.3x5.8 -> Capacitor_SMD:CP_Elec_4x5.8; Manufacturer_Part_Number UCD1H100MCL6GS -> UCD1E100MCL1GS
- C58: renamed from C60; footprint Capacitor_SMD:CP_Elec_6.3x5.8 -> Capacitor_SMD:CP_Elec_4x5.8; Manufacturer_Part_Number UCD1H100MCL6GS -> UCD1E100MCL1GS
- C59: renamed from C61; footprint Capacitor_SMD:CP_Elec_6.3x5.8 -> Capacitor_SMD:CP_Elec_4x5.8; Manufacturer_Part_Number UCD1H100MCL6GS -> UCD1E100MCL1GS
- C60: renamed from C62; footprint Capacitor_SMD:CP_Elec_6.3x5.8 -> Capacitor_SMD:CP_Elec_4x5.8; Manufacturer_Part_Number UCD1H100MCL6GS -> UCD1E100MCL1GS
- C61: renamed from C63; footprint Capacitor_SMD:CP_Elec_6.3x5.8 -> Capacitor_SMD:CP_Elec_4x5.8; Manufacturer_Part_Number UCD1H100MCL6GS -> UCD1E100MCL1GS
- C62: renamed from C64; footprint Capacitor_SMD:CP_Elec_6.3x5.8 -> Capacitor_SMD:CP_Elec_4x5.8; Manufacturer_Part_Number UCD1H100MCL6GS -> UCD1E100MCL1GS
- C63: renamed from C65; footprint Capacitor_SMD:CP_Elec_6.3x5.8 -> Capacitor_SMD:CP_Elec_4x5.8; Manufacturer_Part_Number UCD1H100MCL6GS -> UCD1E100MCL1GS
- renumbered C102 to C100, C103 to C101, C104 to C102, C105 to C103, C106 to C104, C107 to C105, C108 to C106, C109 to C107, C110 to C108, C111 to C109, C13 to C11, C112 to C110, C113 to C111, C114 to C112, C115 to C113, C116 to C114, C117 to C115, C118 to C116, C119 to C117, C120 to C118, C121 to C119, C14 to C12, C122 to C120, C123 to C121, C124 to C122, C125 to C123, C126 to C124, C127 to C125, C128 to C126, C129 to C127, C130 to C128, C131 to C129, C15 to C13, C132 to C130, C133 to C131, C134 to C132, C135 to C133, C136 to C134, C137 to C135, C138 to C136, C139 to C137, C140 to C138, C141 to C139, C142 to C140, C143 to C141, C144 to C142, C145 to C143, C146 to C144, C147 to C145, C148 to C146, C149 to C147, C150 to C148, C151 to C149, C17 to C15, C152 to C150, C153 to C151, C154 to C152, C155 to C153, C156 to C154, C157 to C155, C158 to C156, C159 to C157, C160 to C158, C161 to C159, C18 to C16, C162 to C160, C163 to C161, C164 to C162, C165 to C163, C166 to C164, C167 to C165, C168 to C166, C169 to C167, C170 to C168, C171 to C169, C172 to C170, C173 to C171, C174 to C172, C175 to C173, C20 to C18, C21 to C19, C7 to C5, C8 to C6, C66 to C64, C67 to C65, C68 to C66, C69 to C67, C70 to C68, C71 to C69, C9 to C7, C72 to C70, C73 to C71, C74 to C72, C75 to C73, C76 to C74, C77 to C75, C78 to C76, C79 to C77, C80 to C78, C81 to C79, C10 to C8, C82 to C80, C83 to C81, C84 to C82, C85 to C83, C86 to C84, C87 to C85, C88 to C86, C89 to C87, C90 to C88, C91 to C89, C11 to C9, C92 to C90, C93 to C91, C94 to C92, C95 to C93, C96 to C94, C97 to C95, C98 to C96, C99 to C97, C100 to C98, C101 to C99
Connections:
- net GND: now also C174.2, C175.2
- new net VCC: C174.1, C175.1
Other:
- note added: "Bypass Capacitors"
